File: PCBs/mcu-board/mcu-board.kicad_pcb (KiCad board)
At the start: 2 copper layers, 6 parts, among them J1 ENCODER-PANEL-1, J2 ENCODER-PANEL-2, J3 5V, J4 3.3V, J5 MDAC-INPUT-SELECTOR, U1 m0-express

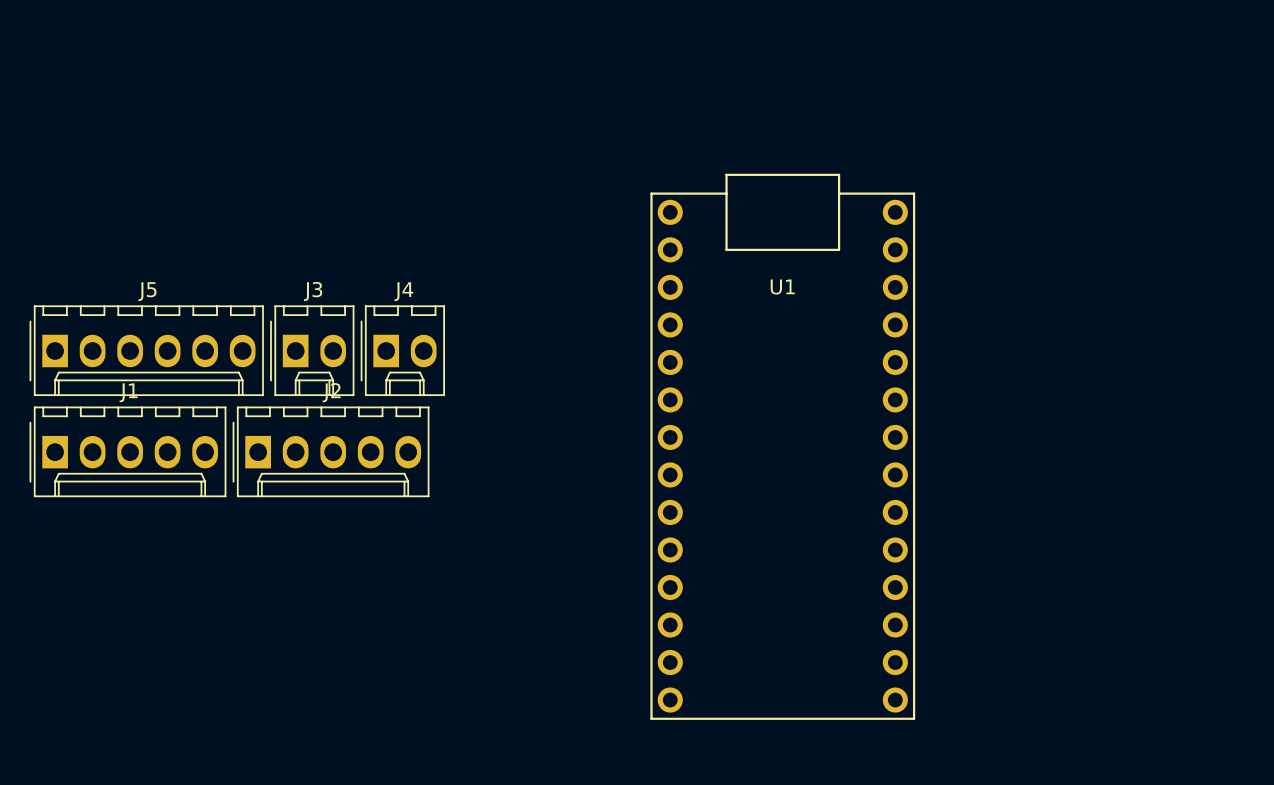
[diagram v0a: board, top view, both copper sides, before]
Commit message: Addinng PCB for MCU board (#8)
* Updating mcu-board PCB

* renaming some nets

* starting to fix silkscreen

* change pad/mask clearance

* misc updates

* adding images

* update readme
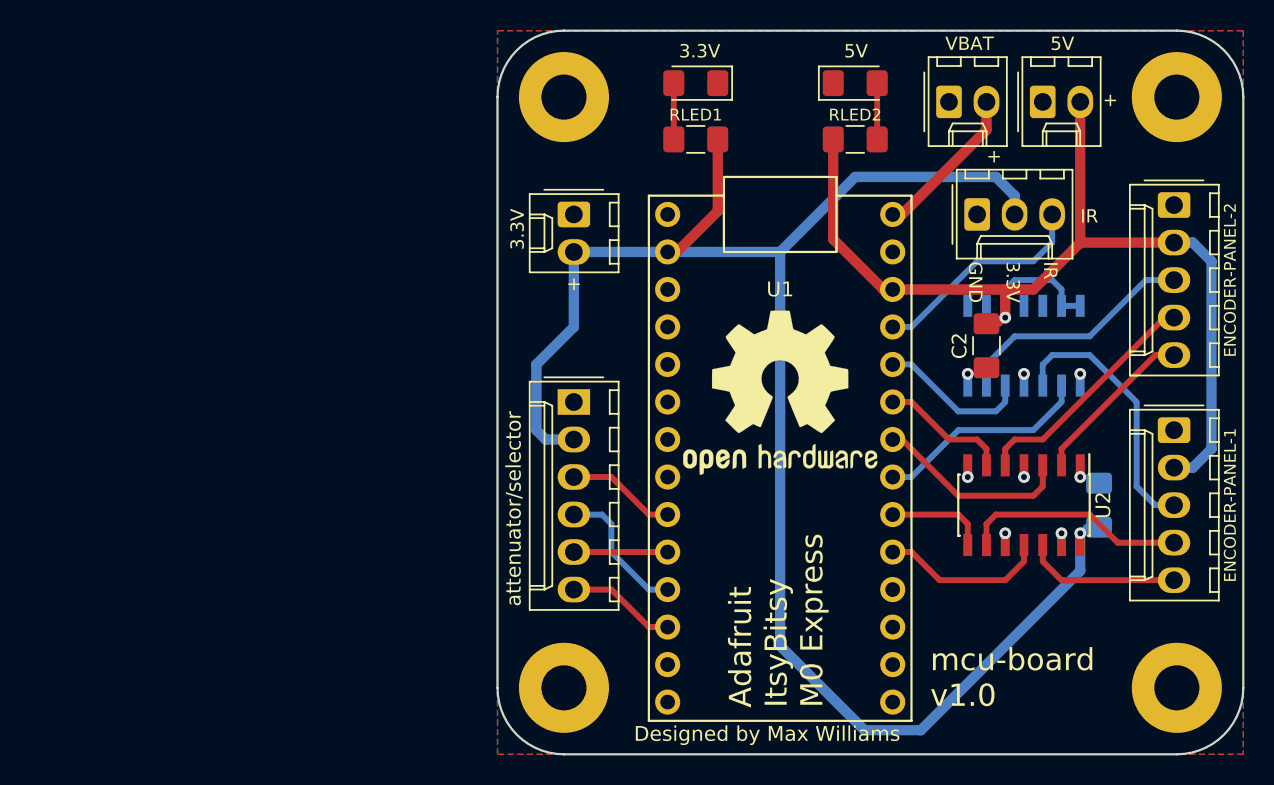
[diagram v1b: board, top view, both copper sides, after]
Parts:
- removed J1: ENCODER-PANEL-1, Connector_Molex:Molex_KK-254_AE-6410-05A_1x05_P2.54mm_Vertical
- removed J2: ENCODER-PANEL-2, Connector_Molex:Molex_KK-254_AE-6410-05A_1x05_P2.54mm_Vertical
- removed J3: 5V, Connector_Molex:Molex_KK-254_AE-6410-02A_1x02_P2.54mm_Vertical
- removed J4: 3.3V, Connector_Molex:Molex_KK-254_AE-6410-02A_1x02_P2.54mm_Vertical
- added 3.3V1: 3.3V, Connector_Molex:Molex_KK-254_AE-6410-02A_1x02_P2.54mm_Vertical, F.Cu at (153.7, 67.9)
- added 5V1: 5V, Connector_Molex:Molex_KK-254_AE-6410-02A_1x02_P2.54mm_Vertical, F.Cu at (185.4, 60.3)
- added C1: C, Capacitor_SMD:C_1206_3216Metric_Pad1.42x1.75mm_HandSolder, B.Cu at (189.2, 87.6)
- added C2: C, Capacitor_SMD:C_1206_3216Metric_Pad1.42x1.75mm_HandSolder, F.Cu at (181.6, 76.8)
- added ENCODER-PANEL-1: ENCODER-PANEL-1, Connector_Molex:Molex_KK-254_AE-6410-05A_1x05_P2.54mm_Vertical, F.Cu at (194.3, 82.5)
- added ENCODER-PANEL-2: ENCODER-PANEL-2, Connector_Molex:Molex_KK-254_AE-6410-05A_1x05_P2.54mm_Vertical, F.Cu at (194.3, 67.3)
- added H1: MountingHole_Pad, MountingHole:MountingHole_3.2mm_M3_Pad, F.Cu at (194.5, 100.0)
- added H2: MountingHole_Pad, MountingHole:MountingHole_3.2mm_M3_Pad, F.Cu at (153.0, 100.0)
- added H3: MountingHole_Pad, MountingHole:MountingHole_3.2mm_M3_Pad, F.Cu at (194.5, 60.0)
- added H4: MountingHole_Pad, MountingHole:MountingHole_3.2mm_M3_Pad, F.Cu at (153.0, 60.0)
- added IR1: Conn_01x03, Connector_Molex:Molex_KK-254_AE-6410-03A_1x03_P2.54mm_Vertical, F.Cu at (181.0, 67.9)
- added LED_3V1: LED, LED_SMD:LED_1206_3216Metric_Pad1.42x1.75mm_HandSolder, F.Cu at (161.9, 59.1)
- added LED_5V1: LED, LED_SMD:LED_1206_3216Metric_Pad1.42x1.75mm_HandSolder, F.Cu at (172.7, 59.1)
- added LOGO1: Logo_Open_Hardware_Small, Symbol:OSHW-Logo2_14.6x12mm_SilkScreen, F.Cu at (167.6, 80.0)
- added LOGO2: Logo_Open_Hardware_Small, Symbol:OSHW-Logo2_14.6x12mm_SilkScreen, B.Cu at (167.6, 69.8)
- added RLED1: R, Resistor_SMD:R_1206_3216Metric_Pad1.42x1.75mm_HandSolder, F.Cu at (161.9, 62.9)
- added RLED2: R, Resistor_SMD:R_1206_3216Metric_Pad1.42x1.75mm_HandSolder, F.Cu at (172.7, 62.9)
- added U2: SN74AHCT125DR, Package_SO:SOIC-14_3.9x8.7mm_P1.27mm, F.Cu at (184.2, 87.6)
- added U3: SN74AHCT125DR, Package_SO:SOIC-14_3.9x8.7mm_P1.27mm, B.Cu at (184.2, 76.8)
- added VBAT1: V-BAT, Connector_Molex:Molex_KK-254_AE-6410-02A_1x02_P2.54mm_Vertical, F.Cu at (179.1, 60.3)
- moved J5 35.3 mm to (153.7, 80.6), turned to 270 degrees
- moved U1 0.23 mm to (167.6, 85.7)
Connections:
- J5 pad 1: Net-(J5-Pad1) -> GND
- J5 pad 2: Net-(J5-Pad2) -> +3V3
- J5 pad 3: Net-(J5-Pad3) -> CS_input_selector
- J5 pad 4: Net-(J5-Pad4) -> SCK
- J5 pad 5: Net-(J5-Pad5) -> CS_mdac_attenuator
- J5 pad 6: Net-(J5-Pad6) -> MOSI
- U1 pad 10: Net-(U1-Pad10) -> CS_mdac_attenuator
- U1 pad 11: Net-(U1-Pad11) -> SCK
- U1 pad 12: Net-(U1-Pad12) -> MOSI
- U1 pad 19: Net-(U1-Pad19) -> panel_1_encoder_A_3v
- U1 pad 2: Net-(U1-Pad2) -> +3V3
- U1 pad 20: Net-(U1-Pad20) -> panel_1_encoder_B_3v
- U1 pad 21: Net-(U1-Pad21) -> panel_1_neopixel_3v
- U1 pad 22: Net-(U1-Pad22) -> panel_2_encoder_A_3v
- U1 pad 23: Net-(U1-Pad23) -> panel_2_encoder_B_3v
- U1 pad 24: Net-(U1-Pad24) -> panel_2_neopixel_3v
- U1 pad 25: Net-(U1-Pad25) -> IR_SENSOR
- U1 pad 26: Net-(U1-Pad26) -> +5V
- U1 pad 27: Net-(U1-Pad27) -> GND
- U1 pad 28: Net-(U1-Pad28) -> BAT
- U1 pad 9: Net-(U1-Pad9) -> CS_input_selector
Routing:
- net +3V3: track 0.00 -> 117.7 mm, vias 0 -> 1
- net +5V: track 0.00 -> 72.9 mm, vias 0 -> 1
- net panel_1_neopixel_5v: track 0.00 -> 18.1 mm
- net panel_2_neopixel_5v: track 0.00 -> 16.5 mm
- net panel_2_encoder_B_5v: track 0.00 -> 16.2 mm
- net panel_1_encoder_B_5v: track 0.00 -> 15.2 mm
- net IR_SENSOR: track 0.00 -> 15.1 mm
- net panel_1_neopixel_3v: track 0.00 -> 14.6 mm
- net panel_2_encoder_A_3v: track 0.00 -> 13.4 mm
- net panel_2_encoder_A_5v: track 0.00 -> 11.4 mm
- net panel_1_encoder_A_3v: track 0.00 -> 11.3 mm
- net BAT: track 0.00 -> 10.6 mm
- net panel_1_encoder_A_5v: track 0.00 -> 10.5 mm
- net panel_2_neopixel_3v: track 0.00 -> 10.3 mm
- net SCK: track 0.00 -> 9.57 mm
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- added copper zone on B.Cu, net GND
- added copper zone on F.Cu, net GND
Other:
- board outline added: 50.5 x 49 mm
- net class Default: clearance 0.2 -> 0.1524; trace_width 0.25 -> 0.4
- net class power added: clearance 0.1524, trace_width 0.7, via_dia 0.8, via_drill 0.4
- rule pad_to_mask_clearance: 0.2 -> 0.0508
- rule trace_clearance: 0.2 -> 0.1524
- rule trace_min: 0.2 -> 0.1524
- rule via_min_drill: 0.3 -> 0.3302
- rule via_min_size: 0.4 -> 0.6858
- board text added: "+"
- board text added: "3.3V"
- board text added: "5V"
- board text added: "Adafruit ItsyBitsy M0 Express"
- board text added: "Designed by Max Williams"
- board text added: "GND"
- board text added: "IR"
- board text added: "VBAT"
- board text added: "attenuator/selector"
- board text added: "futuresharks@gmail.com"
- board text added: "github.com/FutureSharks/preamp-two"
- board text added: "mcu-board v1.0"

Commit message: Updating mcu-board to not use pin 5
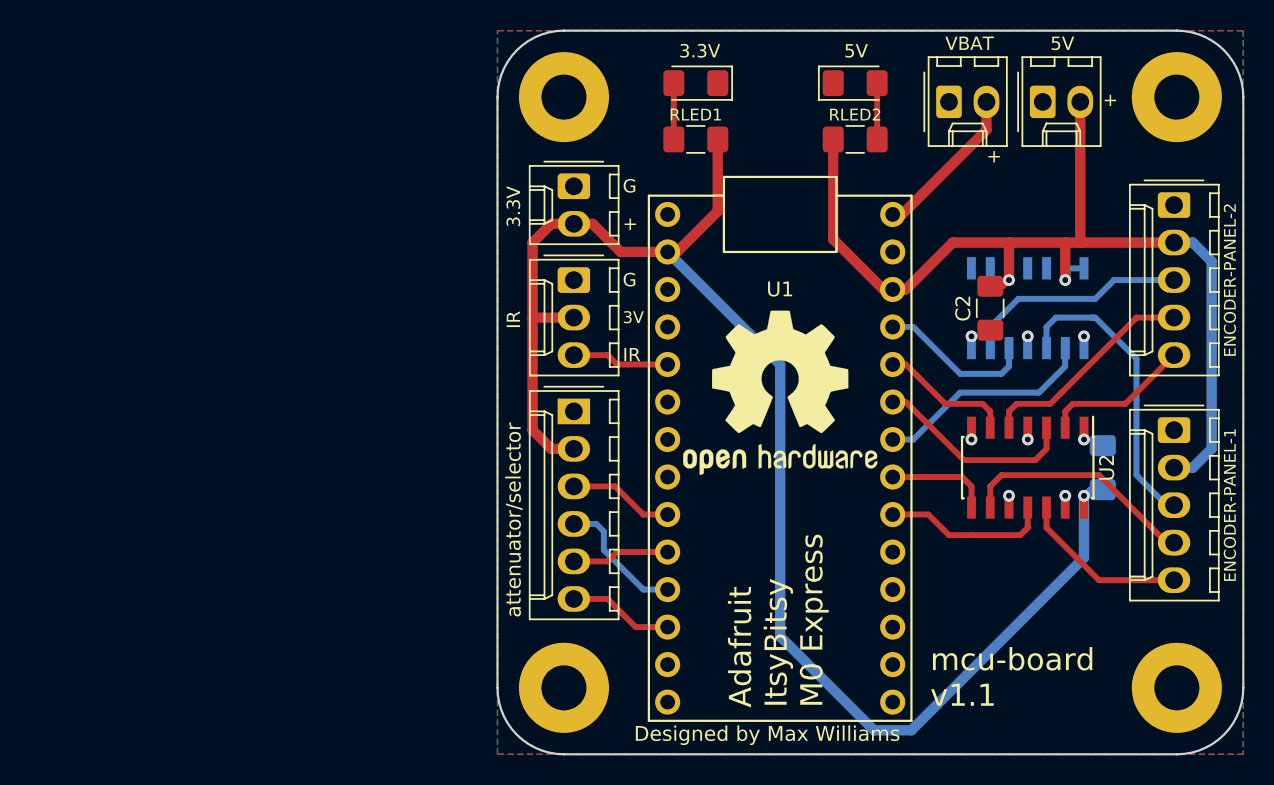
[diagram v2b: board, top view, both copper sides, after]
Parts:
- moved IR1 27.7 mm to (153.7, 72.4), turned to 270 degrees
- moved C1 2.55 mm to (189.5, 85.1)
- moved C2 2.55 mm to (181.9, 74.3)
- moved U2 2.55 mm to (184.4, 85.1)
- moved U3 2.55 mm to (184.4, 74.3)
- moved 3.3V1 1.90 mm to (153.7, 66.0)
- moved J5 0.64 mm to (153.7, 81.3)
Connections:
- U1 pad 19: panel_1_encoder_A_3v -> Net-(U1-Pad19)
- U1 pad 20: panel_1_encoder_B_3v -> panel_1_encoder_A_3v
- U1 pad 21: panel_1_neopixel_3v -> panel_1_encoder_B_3v
- U1 pad 22: panel_2_encoder_A_3v -> panel_1_neopixel_3v
- U1 pad 23: panel_2_encoder_B_3v -> panel_2_encoder_A_3v
- U1 pad 24: panel_2_neopixel_3v -> panel_2_encoder_B_3v
- U1 pad 25: IR_SENSOR -> panel_2_neopixel_3v
- U1 pad 5: Net-(U1-Pad5) -> IR_SENSOR
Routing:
- net +3V3: track 117.7 -> 102.3 mm
- net IR_SENSOR: track 15.1 -> 6.61 mm
- net +5V: track 72.9 -> 70.3 mm, vias 1 -> 2
- net panel_1_neopixel_5v: track 18.1 -> 20.3 mm
- net panel_2_encoder_A_5v: track 11.4 -> 10.1 mm
- net panel_2_neopixel_5v: track 16.5 -> 15.3 mm
- net panel_1_neopixel_3v: track 14.6 -> 15.6 mm
- net panel_1_encoder_A_5v: track 10.5 -> 11.5 mm
- net panel_1_encoder_B_5v: track 15.2 -> 16.1 mm
- net panel_2_encoder_B_5v: track 16.2 -> 15.6 mm
- net SCK: track 9.57 -> 8.94 mm
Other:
- board text added: "3V"
- board text added: "G"
- board text added: "mcu-board v1.1"
- board text removed: "GND"
- board text removed: "mcu-board v1.0"
